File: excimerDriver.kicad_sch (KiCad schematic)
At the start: 47 parts, among them IC3 INA210, IC6 STM32G071KBT6, J1 B08B-XASK-1-A_LF__SN_, J3 BM02B-SRSS-TB_LF__SN_, J4 BM02B-SRSS-TB_LF__SN_, J6 640445-2, Q3 BSS138, U4 Prog

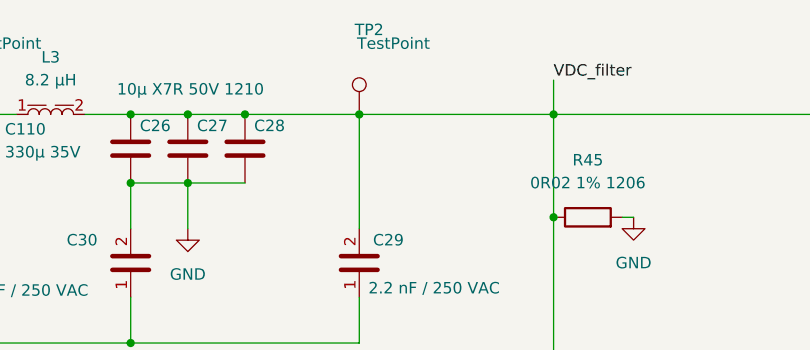
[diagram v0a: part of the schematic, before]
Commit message: prototyp V2 with bug fixes
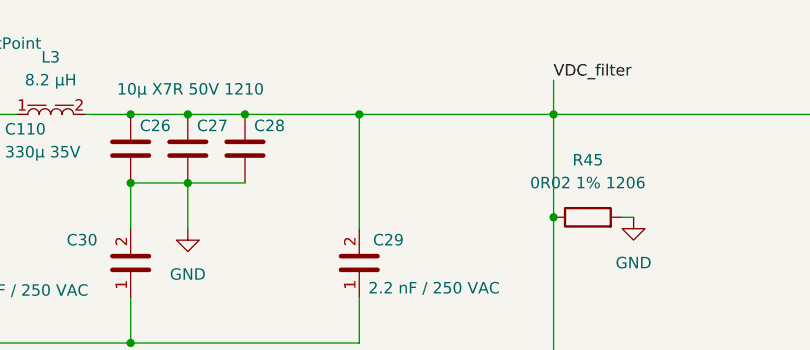
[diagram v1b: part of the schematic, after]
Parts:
- removed TP2: TestPoint, TestPoint:TestPoint_Pad_D1.0mm, symbol Connector:TestPoint
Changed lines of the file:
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@@
-	)
-	(symbol
-		(lib_id "Connector:TestPoint")
-		(at 107.95 25.4 0)
-		(unit 1)
-		(exclude_from_sim no)
-		(in_bom yes)
-		(on_board yes)
-		(dnp no)
-		(property "Reference" "TP2"
-			(at 107.442 16.002 0)
-			(effects
-				(font
-					(size 1.27 1.27)
-				)
-				(justify left)
-			)
-		)
-		(property "Value" "TestPoint"
-			(at 107.696 17.526 0)
-			(effects
-				(font
-					(size 1.27 1.27)
-				)
-				(justify left)
-			)
-		)
-		(property "Footprint" "TestPoint:TestPoint_Pad_D1.0mm"
-			(at 113.03 25.4 0)
-			(effects
-				(font
-					(size 1.27 1.27)
-				)
-				(hide yes)
-			)
-		)
-		(property "Datasheet" ""
-			(at 113.03 25.4 0)
-			(effects
-				(font
-					(size 1.27 1.27)
-				)
-				(hide yes)
-			)
-		)
-		(property "Description" "test point"
-			(at 107.95 25.4 0)
-			(effects
-				(font
-					(size 1.27 1.27)
-				)
-				(hide yes)
-			)
-		)
-		(pin "1"
-		)
-		(instances
-			(project "OSLUV"
-				(path "/c6e900e0-9399-44f0-8089-9dd7b8ffe54c/9b3070c3-43e0-4d43-9da1-9bc1bd2d6fb9"
-					(reference "TP2")
-					(unit 1)
-				)
-			)
-		)
 	)
 	(symbol

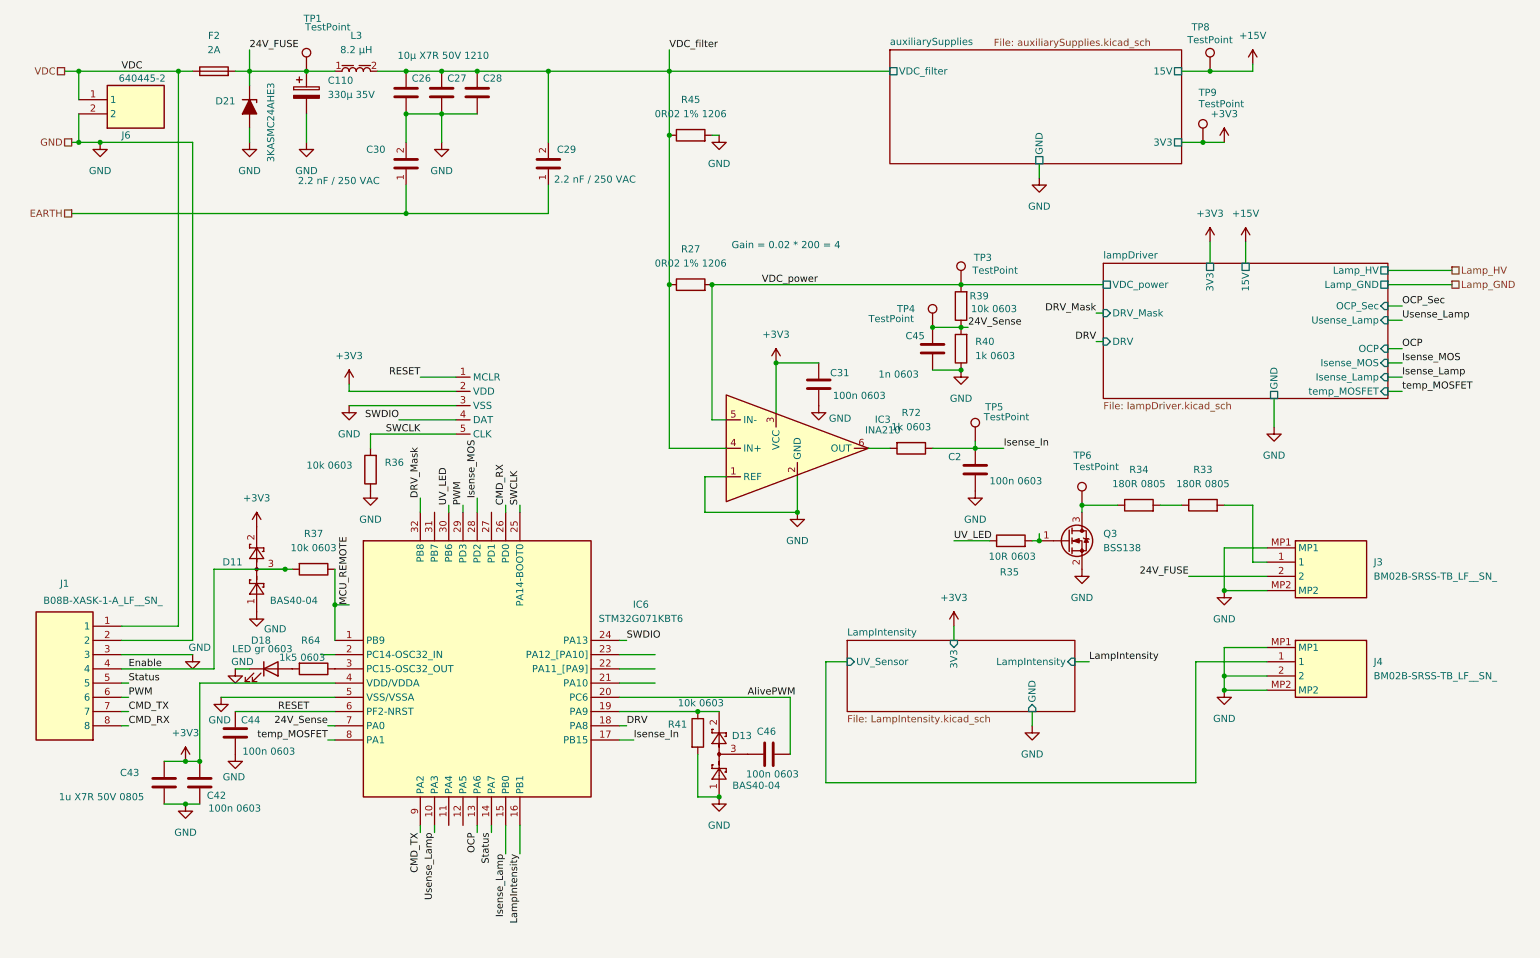
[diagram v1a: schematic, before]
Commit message: prototyp V2 with fixed gate driver, test points placed
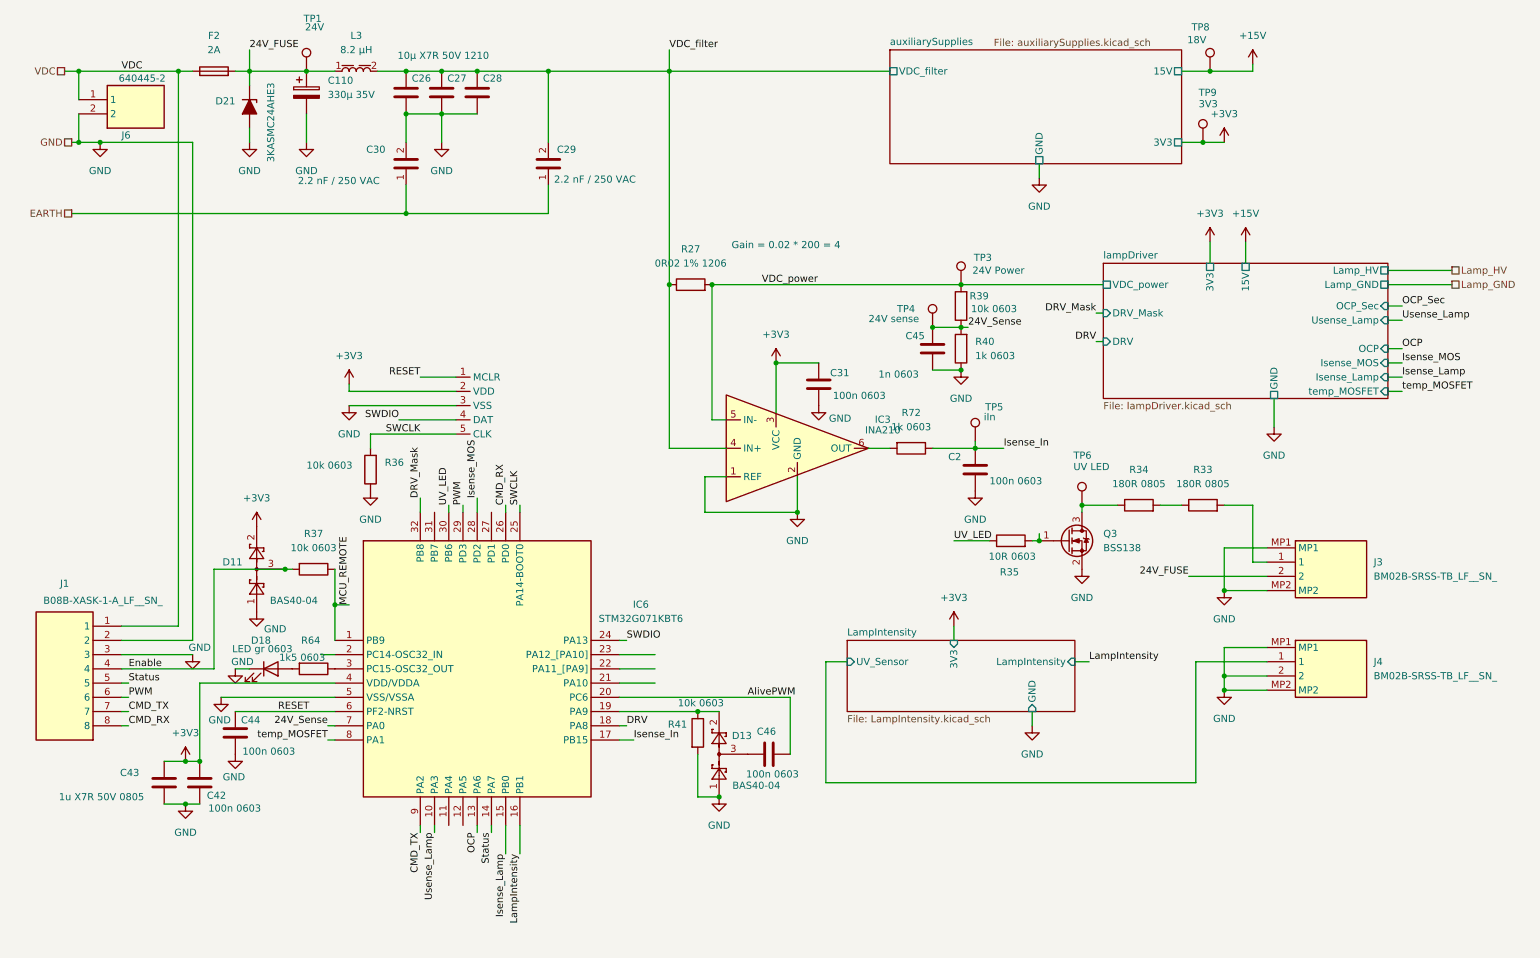
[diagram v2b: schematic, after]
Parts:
- removed R45: 0R02 1% 1206, Resistor_SMD:R_1206_3216Metric, symbol Device:R
- TP1: value TestPoint -> 24V
- TP3: value TestPoint -> 24V Power
- TP4: value TestPoint -> 24V sense
- TP5: value TestPoint -> iIn
- TP6: value TestPoint -> UV LED
- TP8: value TestPoint -> 18V
- TP9: value TestPoint -> 3V3
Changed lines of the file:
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@@
 	)
 	(junction
-		(at 129.54 36.83)
-		(diameter 0)
-		(color 0 0 0 0)
-	)
-	(junction
 		(at 226.06 25.4)
 		(diameter 0)
@@
 	(wire
 		(pts
-			(xy 137.16 36.83) (xy 138.43 36.83)
-		)
-		(stroke
-			(width 0)
-			(type default)
-		)
-	)
-	(wire
-		(pts
 			(xy 24.13 25.4) (xy 41.91 25.4)
 		)
@@
 	(wire
 		(pts
-			(xy 129.54 36.83) (xy 129.54 63.5)
+			(xy 129.54 25.4) (xy 129.54 63.5)
 		)
 		(stroke
@@
 	(wire
 		(pts
-			(xy 129.54 25.4) (xy 129.54 36.83)
-		)
-		(stroke
-			(width 0)
-			(type default)
-		)
-	)
-	(wire
-		(pts
 			(xy 45.72 134.62) (xy 45.72 148.59)
 		)
@@
 			)
 		)
-		(property "Value" "TestPoint"
+		(property "Value" "UV LED"
 			(at 201.676 96.012 0)
 			(effects
@@
 			)
 		)
-		(property "Value" "TestPoint"
+		(property "Value" "24V"
 			(at 64.516 17.526 0)
 			(effects
@@
 			)
 		)
-		(property "Value" "TestPoint"
+		(property "Value" "18V"
 			(at 221.996 19.812 0)
 			(effects
@@
 			)
 		)
-		(property "Value" "TestPoint"
+		(property "Value" "iIn"
 			(at 185.674 87.122 0)
 			(effects
@@
 			)
 		)
-		(property "Value" "TestPoint"
+		(property "Value" "24V sense"
 			(at 165.1 69.596 0)
 			(effects
@@
 			)
 		)
-		(property "Value" "TestPoint"
+		(property "Value" "24V Power"
 			(at 183.642 60.96 0)
 			(effects
@@
 	(symbol
 		(lib_id "power:GND")
-		(at 138.43 36.83 0)
-		(unit 1)
-		(exclude_from_sim no)
-		(in_bom yes)
-		(on_board yes)
-		(dnp no)
-		(fields_autoplaced yes)
-		(property "Reference" "#PWR079"
-			(at 138.43 43.18 0)
-			(effects
-				(font
-					(size 1.27 1.27)
-				)
-				(hide yes)
-			)
-		)
-		(property "Value" "GND"
-			(at 138.43 41.91 0)
-			(effects
-				(font
-					(size 1.27 1.27)
-				)
-			)
-		)
-		(property "Footprint" ""
-			(at 138.43 36.83 0)
-			(effects
-				(font
-					(size 1.27 1.27)
-				)
-				(hide yes)
-			)
-		)
-		(property "Datasheet" ""
-			(at 138.43 36.83 0)
-			(effects
-				(font
-					(size 1.27 1.27)
-				)
-				(hide yes)
-			)
-		)
-		(property "Description" "Power symbol creates a global label with name \"GND\" , ground"
-			(at 138.43 36.83 0)
-			(effects
-				(font
-					(size 1.27 1.27)
-				)
-				(hide yes)
-			)
-		)
-		(pin "1"
-		)
-		(instances
-			(project "OSLUV"
-				(path "/c6e900e0-9399-44f0-8089-9dd7b8ffe54c/9b3070c3-43e0-4d43-9da1-9bc1bd2d6fb9"
-					(reference "#PWR079")
-					(unit 1)
-				)
-			)
-		)
-	)
-	(symbol
-		(lib_id "Device:R")
-		(at 133.35 36.83 90)
-		(unit 1)
-		(exclude_from_sim no)
-		(in_bom yes)
-		(on_board yes)
-		(dnp no)
-		(fields_autoplaced yes)
-		(property "Reference" "R45"
-			(at 133.35 30.48 90)
-			(effects
-				(font
-					(size 1.27 1.27)
-				)
-			)
-		)
-		(property "Value" "0R02 1% 1206"
-			(at 133.35 33.02 90)
-			(effects
-				(font
-					(size 1.27 1.27)
-				)
-			)
-		)
-		(property "Footprint" "Resistor_SMD:R_1206_3216Metric"
-			(at 133.35 38.608 90)
-			(effects
-				(font
-					(size 1.27 1.27)
-				)
-				(hide yes)
-			)
-		)
-		(property "Datasheet" ""
-			(at 133.35 36.83 0)
-			(effects
-				(font
-					(size 1.27 1.27)
-				)
-				(hide yes)
-			)
-		)
-		(property "Description" "Resistor"
-			(at 133.35 36.83 0)
-			(effects
-				(font
-					(size 1.27 1.27)
-				)
-				(hide yes)
-			)
-		)
-		(pin "1"
-		)
-		(pin "2"
-		)
-		(instances
-			(project "OSLUV"
-				(path "/c6e900e0-9399-44f0-8089-9dd7b8ffe54c/9b3070c3-43e0-4d43-9da1-9bc1bd2d6fb9"
-					(reference "R45")
-					(unit 1)
-				)
-			)
-		)
-	)
-	(symbol
-		(lib_id "power:GND")
 		(at 76.2 100.33 0)
 		(unit 1)
@@
 			)
 		)
-		(property "Value" "TestPoint"
+		(property "Value" "3V3"
 			(at 224.028 31.242 0)
 			(effects

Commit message: Rev. 1.0.0 production data
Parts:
- removed C46: 100n 0603, Capacitor_SMD:C_0603_1608Metric, symbol Device:C
- removed D11, D13: BAS40-04, Package_TO_SOT_SMD:SOT-23, symbol Diode:BAS40-04
- removed J4: BM02B-SRSS-TB_LF__SN_, Hansmann:BM02BSRSSTBLFSN, symbol Hansmann:BM02B-SRSS-TB_LF__SN_
- removed J6: 640445-2, 6404452, symbol Hansmann:640445-2
- removed U4: Prog, Hansmann:Prog_St, symbol Hansmann:Prog_ST
- added C28, C29: 100n 0603, Capacitor_SMD:C_0603_1608Metric, symbol Device:C
- added D11: LED rd 0603, LED_SMD:LED_0603_1608Metric, symbol Device:LED
- added D13, D14: D5V0P4UR6SO-7, SOT95P285X140-6N, symbol Hansmann_Dioden:D5V0P4UR6SO-7
- added F2: Polyfuse 200 mA, Fuse:Fuse_1206_3216Metric, symbol Device:Fuse
- added J1: B04B-XASK-1_LF__SN_, B04BXASK1LFSN, symbol Hansmann_Connectors:B04B-XASK-1_LF__SN_
- added J3: TC2030, Connector:Tag-Connect_TC2030-IDC-NL_2x03_P1.27mm_Vertical_beidseitig, symbol Connector:TC2030
- added J5: B4B-PH-K-S_LF__SN_, Hansmann_Kontakte:B4B-PH-K-S, symbol Hansmann_Connectors:B4B-PH-K-S_LF__SN_
- added L2: L, Inductor_SMD:L_0805_2012Metric, symbol Device:L
- added Q2: DCX114EU-7-F, SOT65P210X110-6N, symbol Hansmann_Transistoren:DCX114EU-7-F
- added R28, R29, R30, R44, R45: 100R 0603, Resistor_SMD:R_0603_1608Metric, symbol Device:R
- added R31: 1k5 0603, Resistor_SMD:R_0603_1608Metric, symbol Device:R
- added R34: 10k 0603, Resistor_SMD:R_0603_1608Metric, symbol Device:R
- added R40: 2k2 0603, Resistor_SMD:R_0603_1608Metric, symbol Device:R
- C2: renamed from C110; value 330µ 35V -> 100µ 35V; footprint Capacitor_THT:CP_Radial_D8.0mm_P5.00mm -> Capacitor_THT:CP_Radial_D8.0mm_P3.50mm
- J2: renamed from J1; footprint Hansmann:B08BXASK1ALFSN -> Connector_JST:JST_XA_B08B-XASK-1-A_1x08_P2.50mm_Vertical
- R27: renamed from R37; value 10k 0603 -> 1k 0603
- R41: value 10k 0603 -> 2k2 0603
- R42: renamed from R34; value 180R 0805 -> 680R 0805
- R43: renamed from R33; value 180R 0805 -> 680R 0805
- renumbered C43 to C1, C27 to C16, C28 to C17, C29 to C24, C31 to C25, C45 to C26, C2 to C27, C42 to C3, C44 to C4, C26 to C5, C30 to C6, D21 to D10, D18 to D12, F2 to F1, IC6 to IC3, IC3 to IC4, J3 to J4, L3 to L1, R64 to R32, R36 to R33, R27 to R35, R72 to R36, R39 to R37, R40 to R38, R35 to R39, TP4 to TP2, TP5 to TP4, TP6 to TP5, TP9 to TP6, TP8 to TP7
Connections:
- net LampIntensity is gone; now on net Usense_Lamp: IC3.16 (PB1)
- net +3V3: now also R41.2, C28.2, D13.5 (VCC), D14.5 (VCC), J3.1, L2.1, R40.2
- net CMD_RX: now also IC3.10 (PA3), D13.4 (I/O3), R28.2; no longer IC3.26 (PD0), J2.8
- net CMD_TX: now also D13.6 (I/O4), R30.2; no longer J2.7
- net GND: now also C28.1, C29.1, D11.1 (K), D13.2 (VSS), D14.2 (VSS), J1.4, J3.5, J5.4, Q2.1 (COM1), R34.1; no longer R41.2
- net MCU_REMOTE: now also D14.3 (I/O2)
- net PWM: now also D13.3 (I/O2), R29.2, R34.2; no longer J2.6
- net RESET: now also J3.3
- net SWCLK: now also J3.4
- net SWDIO: now also J3.2
- net Status: now also D13.1 (I/O1), Q2.2 (IN1); no longer J2.5
- net UV_LED: now also IC3.11 (PA4); no longer IC3.30 (PB6)
- net Usense_Lamp: no longer IC3.10 (PA3)
- net VDC: now also J1.1
- net at IC3.19 (PA9): no longer R41.1
- net LED2: now reaches IC3.2 (PC14-OSC32_IN)
- net LED2: now also R31.1
- net I2C_SCL: now reaches IC3.22 (PA11_[PA9])
- net I2C_SCL: now also R41.1, D14.4 (I/O3), R44.1
- net I2C_SDA: now reaches IC3.23 (PA12_[PA10])
- net I2C_SDA: now also D14.6 (I/O4), R40.1, R45.1
- net LED1: now reaches IC3.3 (PC15-OSC32_OUT), R32.1
- net AlivePWM renamed OCP_RESET
- net DRV_Mask: no longer names the net of IC3.32 (PB8)
- net Enable renamed !REMOTE
- net !REMOTE: now also J1.2
- new net: C29.2, F2.1, L2.2
- new net: F2.2, J5.3
- new net: J2.6, R29.1
- new net: J2.7, R30.1
- new net: J2.8, R28.1
- new net: J5.2, R45.2
- new net: J5.1, R44.2
- new net: D11.2 (A), R31.2
- new net Lamp_on_status: J1.3, J2.5, Q2.6 (OUT1)
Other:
- removed sheet LampIntensity
- sheet lampDriver ports: added OCP_RESET; removed DRV_Mask, OCP_Sec
- moved on the sheet: C1, C3, C4, D12, IC3, J2, R27, R32, R33

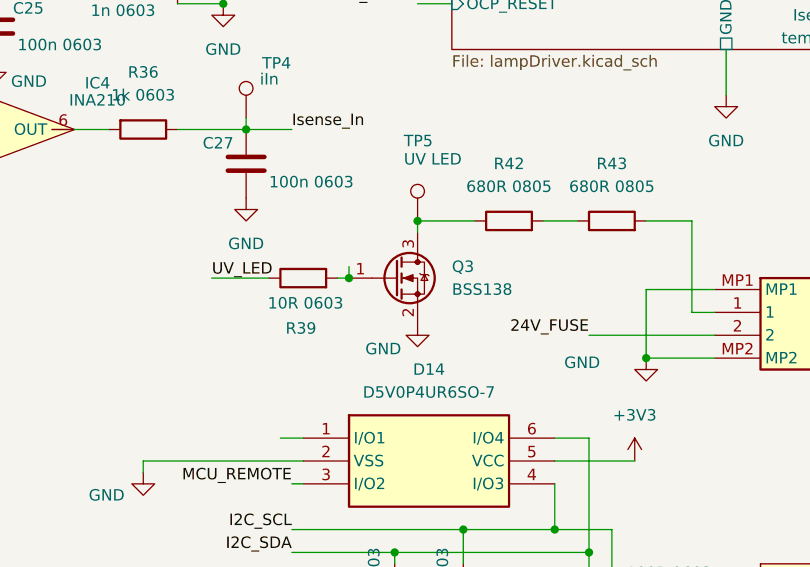
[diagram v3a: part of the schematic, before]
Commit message: Rev 1.0.0 corrected component values
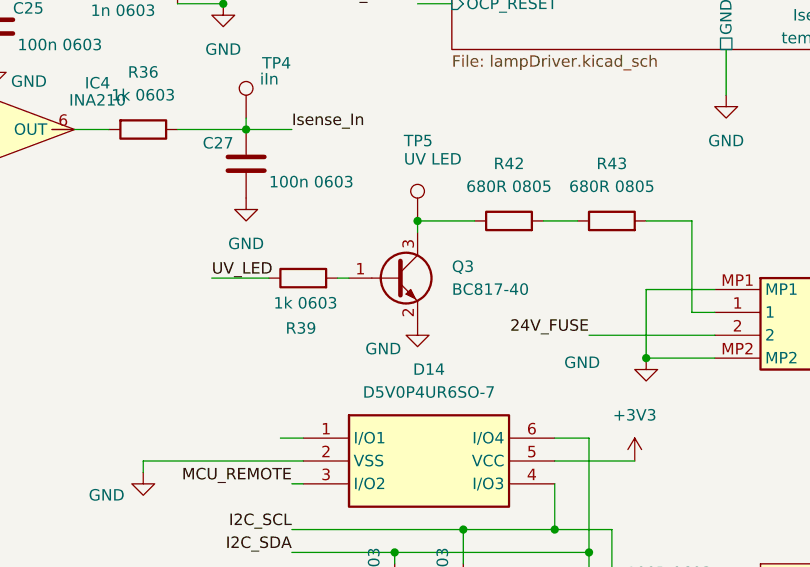
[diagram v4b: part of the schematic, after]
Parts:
- removed Q3: BSS138, Package_TO_SOT_SMD:SOT-23, symbol Transistor_FET:BSS138
- added Q3: BC817-40, Package_TO_SOT_SMD:SOT-23, symbol Transistor_BJT:BC847
- R39: value 10R 0603 -> 1k 0603
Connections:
- net GND: now also Q3.2 (E)
- net at R39.2: now also Q3.1 (B)
- net at R42.1, TP5.1: now also Q3.3 (C)
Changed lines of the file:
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@@
 	)
 	(junction
-		(at 195.58 109.22)
-		(diameter 0)
-		(color 0 0 0 0)
-	)
-	(junction
 		(at 82.55 33.02)
 		(diameter 0)
@@
 	(wire
 		(pts
-			(xy 195.58 107.95) (xy 195.58 109.22)
-		)
-		(stroke
-			(width 0)
-			(type default)
-		)
-	)
-	(wire
-		(pts
 			(xy 129.54 92.71) (xy 139.7 92.71)
 		)
@@
 	)
 	(symbol
-		(lib_id "Transistor_FET:BSS138")
-		(at 200.66 109.22 0)
-		(unit 1)
-		(exclude_from_sim no)
-		(in_bom yes)
-		(on_board yes)
-		(dnp no)
-		(fields_autoplaced yes)
-		(property "Reference" "Q3"
-			(at 207.01 107.9499 0)
-			(effects
-				(font
-					(size 1.27 1.27)
-				)
-				(justify left)
-			)
-		)
-		(property "Value" "BSS138"
-			(at 207.01 110.4899 0)
-			(effects
-				(font
-					(size 1.27 1.27)
-				)
-				(justify left)
-			)
-		)
-		(property "Footprint" "Package_TO_SOT_SMD:SOT-23"
-			(at 205.74 111.125 0)
-			(effects
-				(font
-					(size 1.27 1.27)
-					(italic yes)
-				)
-				(justify left)
-				(hide yes)
-			)
-		)
-		(property "Datasheet" "https://www.onsemi.com/pub/Collateral/BSS138-D.PDF"
-			(at 205.74 113.03 0)
-			(effects
-				(font
-					(size 1.27 1.27)
-				)
-				(justify left)
-				(hide yes)
-			)
-		)
-		(property "Description" "50V Vds, 0.22A Id, N-Channel MOSFET, SOT-23"
-			(at 200.66 109.22 0)
-			(effects
-				(font
-					(size 1.27 1.27)
-				)
-				(hide yes)
-			)
-		)
-		(pin "3"
-		)
-		(pin "2"
-		)
-		(pin "1"
-		)
-		(instances
-			(project ""
-				(path "/c6e900e0-9399-44f0-8089-9dd7b8ffe54c/9b3070c3-43e0-4d43-9da1-9bc1bd2d6fb9"
-					(reference "Q3")
-					(unit 1)
-				)
-			)
-		)
-	)
-	(symbol
 		(lib_id "power:GND")
 		(at 27.94 38.1 0)
@@
 	)
 	(symbol
+		(lib_id "Transistor_BJT:BC847")
+		(at 200.66 109.22 0)
+		(unit 1)
+		(exclude_from_sim no)
+		(in_bom yes)
+		(on_board yes)
+		(dnp no)
+		(property "Reference" "Q3"
+			(at 207.01 107.9499 0)
+			(effects
+				(font
+					(size 1.27 1.27)
+				)
+				(justify left)
+			)
+		)
+		(property "Value" "BC817-40"
+			(at 207.01 110.4899 0)
+			(effects
+				(font
+					(size 1.27 1.27)
+				)
+				(justify left)
+			)
+		)
+		(property "Footprint" "Package_TO_SOT_SMD:SOT-23"
+			(at 205.74 111.125 0)
+			(effects
+				(font
+					(size 1.27 1.27)
+					(italic yes)
+				)
+				(justify left)
+				(hide yes)
+			)
+		)
+		(property "Datasheet" "http://www.infineon.com/dgdl/Infineon-BC847SERIES_BC848SERIES_BC849SERIES_BC850SERIES-DS-v01_01-en.pdf?fileId=db3a304314dca389011541d4630a1657"
+			(at 200.66 109.22 0)
+			(effects
+				(font
+					(size 1.27 1.27)
+				)
+				(justify left)
+				(hide yes)
+			)
+		)
+		(property "Description" "0.1A Ic, 45V Vce, NPN Transistor, SOT-23"
+			(at 200.66 109.22 0)
+			(effects
+				(font
+					(size 1.27 1.27)
+				)
+				(hide yes)
+			)
+		)
+		(pin "2"
+		)
+		(pin "3"
+		)
+		(pin "1"
+		)
+		(instances
+			(project "OSLUV"
+				(path "/c6e900e0-9399-44f0-8089-9dd7b8ffe54c/9b3070c3-43e0-4d43-9da1-9bc1bd2d6fb9"
+					(reference "Q3")
+					(unit 1)
+				)
+			)
+		)
+	)
+	(symbol
 		(lib_id "power:GND")
 		(at 172.72 130.81 0)
@@
 			)
 		)
-		(property "Value" "10R 0603"
+		(property "Value" "1k 0603"
 			(at 190.754 112.014 90)
 			(effects
